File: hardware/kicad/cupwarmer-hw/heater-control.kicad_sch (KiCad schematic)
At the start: 13 parts, among them Q1 AO3400 SOT-23

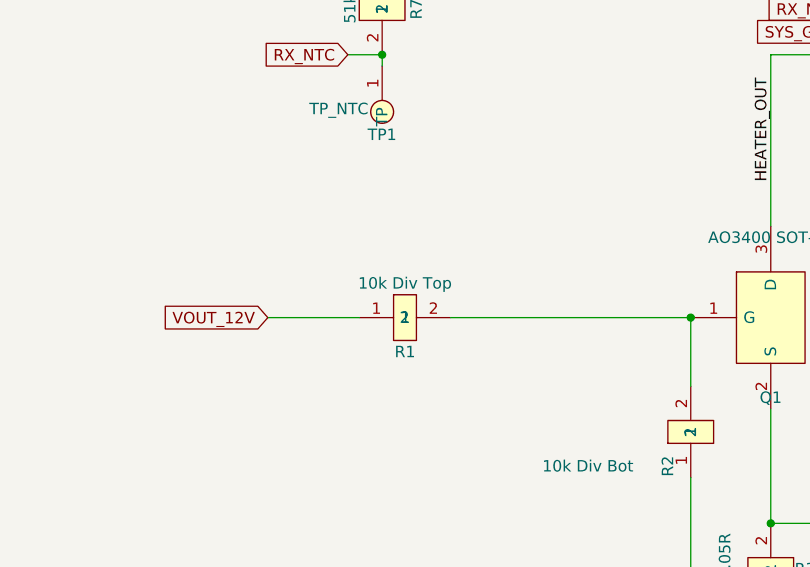
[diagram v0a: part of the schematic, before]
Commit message: Lower heater gate divider voltage
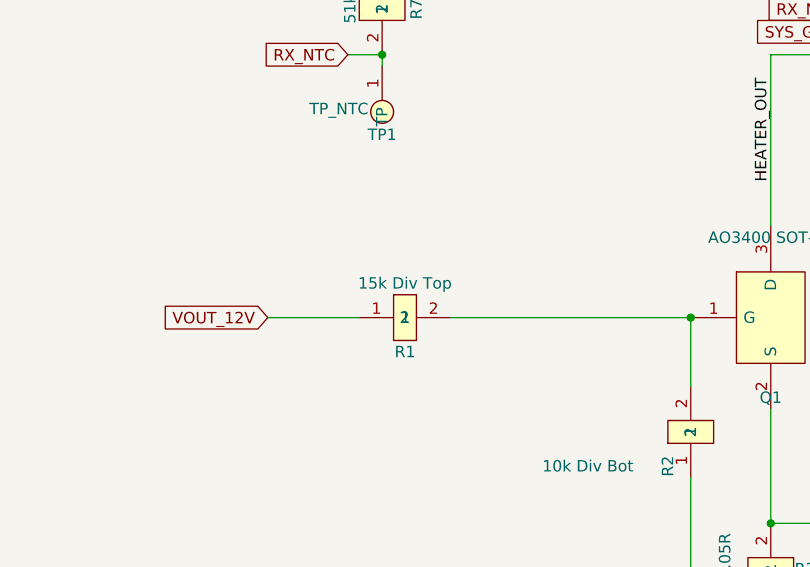
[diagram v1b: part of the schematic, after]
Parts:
- R1: value 10k Div Top -> 15k Div Top; LCSC C25804 -> C22809; MPN 0603WAF1002T5E -> 0603WAF1502T5E
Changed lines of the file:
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@@
 			)
 		)
-		(property "Value" "10k Div Top"
+		(property "Value" "15k Div Top"
 			(at 74.93 87.63 0)
 			(show_name no)
@@
 			)
 		)
-		(property "LCSC" "C25804"
+		(property "LCSC" "C22809"
 			(at 26.67 17.78 0)
 			(hide yes)
@@
 			)
 		)
-		(property "MPN" "0603WAF1002T5E"
+		(property "MPN" "0603WAF1502T5E"
 			(at 26.67 17.78 0)
 			(hide yes)
@@
 			)
 		)
-		(property "Description" "Gate divider bottom (Q1.G -> GND, VGS~=6V)"
+		(property "Description" "Gate divider bottom (Q1.G -> GND, R1/R2=15k/10k gives VGS~=4.8V at VOUT=12V)"
 			(at 106.68 104.14 90)
 			(hide yes)

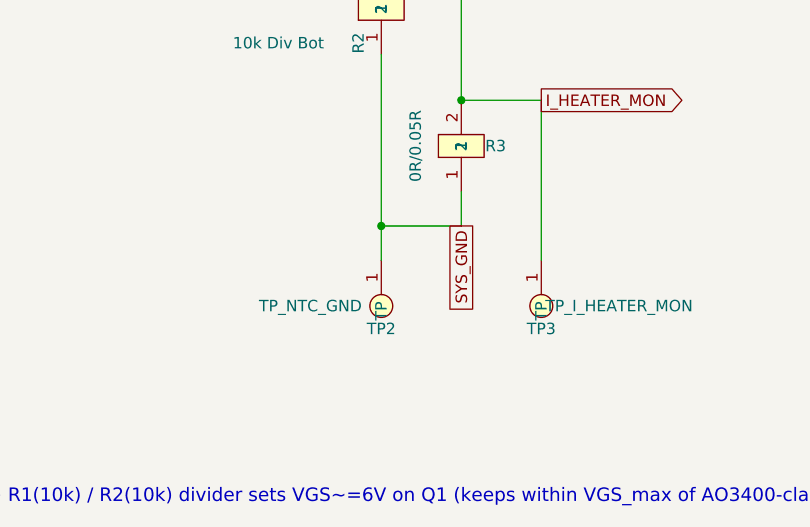
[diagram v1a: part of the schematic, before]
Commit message: Remove redundant NTC ground test point
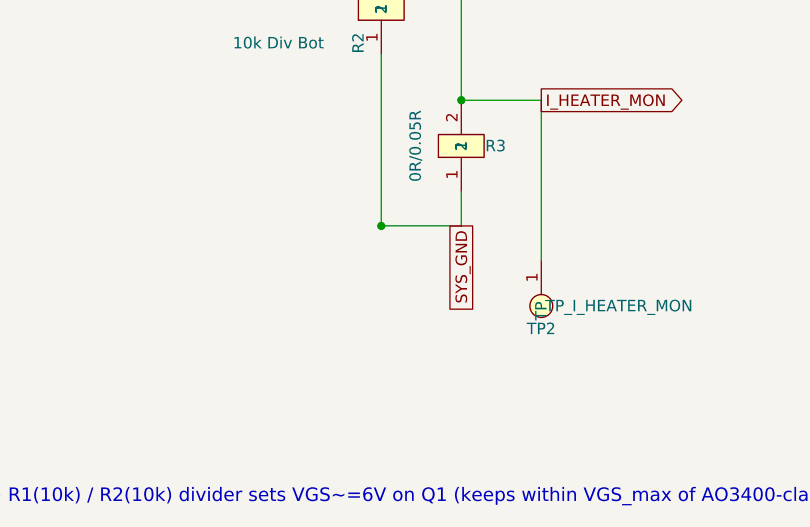
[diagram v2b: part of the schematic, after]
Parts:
- removed TP2: TP_NTC_GND, Connector_PinHeader_2.54mm:PinHeader_1x01_P2.54mm_Vertical, symbol cupwarmer:TESTPAD_1
- renumbered TP3 to TP2
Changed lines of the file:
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@@
-	(wire
-		(pts
-			(xy 106.68 128.27) (xy 106.68 132.08)
-		)
-		(stroke
-			(width 0)
-			(type default)
-		)
-	)
 	(wire
 		(pts
@@
 		(in_pos_files no)
 		(dnp no)
-		(property "Reference" "TP3"
+		(property "Reference" "TP2"
 			(at 124.46 139.7 0)
 			(show_name no)
@@
 			(project "cupwarmer-hw"
 				(path "/f3c63676-f392-4700-9f58-a6787e1eb284/22222222-2222-2222-2222-222222222222"
-					(reference "TP3")
+					(reference "TP2")
 					(unit 1)
 				)
@@
 					(unit 1)
 				)
-			)
-		)
-	)
-	(symbol
-		(lib_id "cupwarmer:TESTPAD_1")
-		(at 106.68 137.16 0)
-		(unit 1)
-		(body_style 1)
-		(exclude_from_sim no)
-		(in_bom no)
-		(on_board yes)
-		(in_pos_files no)
-		(dnp no)
-		(property "Reference" "TP2"
-			(at 106.68 139.7 0)
-			(show_name no)
-			(do_not_autoplace no)
-			(effects
-				(font
-					(size 1.27 1.27)
-				)
-			)
-		)
-		(property "Value" "TP_NTC_GND"
-			(at 98.806 137.16 0)
-			(show_name no)
-			(do_not_autoplace no)
-			(effects
-				(font
-					(size 1.27 1.27)
-				)
-			)
-		)
-		(property "Footprint" "Connector_PinHeader_2.54mm:PinHeader_1x01_P2.54mm_Vertical"
-			(at 106.68 137.16 0)
-			(hide yes)
-			(show_name no)
-			(do_not_autoplace no)
-			(effects
-				(font
-					(size 1.27 1.27)
-				)
-			)
-		)
-		(property "Datasheet" "~"
-			(at 106.68 137.16 0)
-			(hide yes)
-			(show_name no)
-			(do_not_autoplace no)
-			(effects
-				(font
-					(size 1.27 1.27)
-				)
-			)
-		)
-		(property "Description" "DMM return pad for heater NTC before powered test"
-			(at 106.68 137.16 0)
-			(hide yes)
-			(show_name no)
-			(do_not_autoplace no)
-			(effects
-				(font
-					(size 1.27 1.27)
-				)
-			)
-		)
-		(pin "1"
-		)
-		(instances
-			(project "cupwarmer-hw"
-				(path "/f3c63676-f392-4700-9f58-a6787e1eb284/22222222-2222-2222-2222-222222222222"
-					(reference "TP2")
-					(unit 1)
-				)

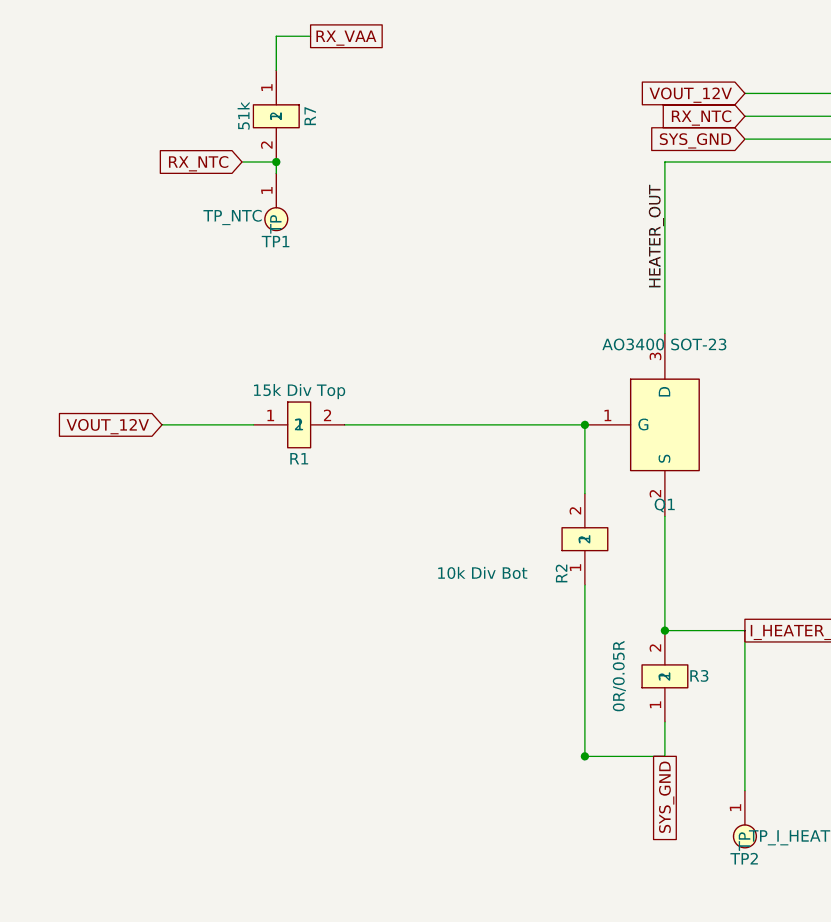
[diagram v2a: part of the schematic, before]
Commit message: Fix LED polarity and heater flyback diode
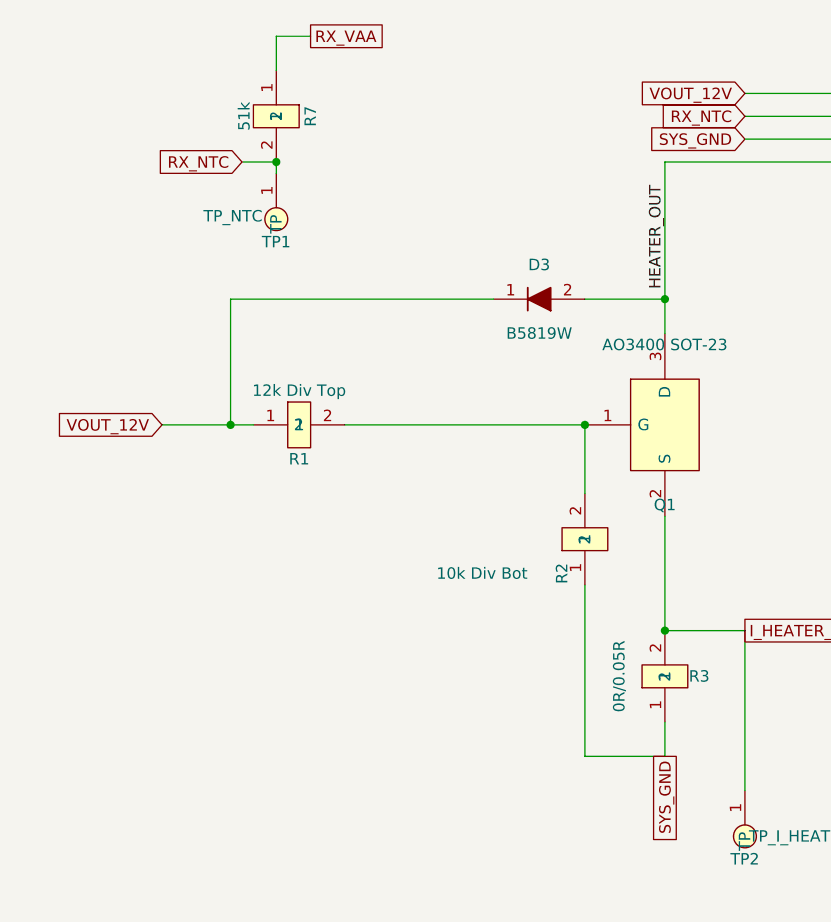
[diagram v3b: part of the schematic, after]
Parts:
- added D3: B5819W, Diode_SMD:D_SOD-123, symbol cupwarmer:DIODE_2
- R1: value 15k Div Top -> 12k Div Top; LCSC C22809 -> C22790; MPN 0603WAF1502T5E -> 0603WAF1202T5E
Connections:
- net HEATER_OUT: now also D3.2 (A)
- net VOUT_12V: now also D3.1 (K)
